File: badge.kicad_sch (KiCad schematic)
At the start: 26 parts, among them J1 SAO V.1.69bis master, SW1 power, SW2 SW_Push, SW3 update epaper, U1 Seeed XIAO ESP32-C3, U2 epaper2.13, U3 5V boost converter, U4 TXS0104EPWR

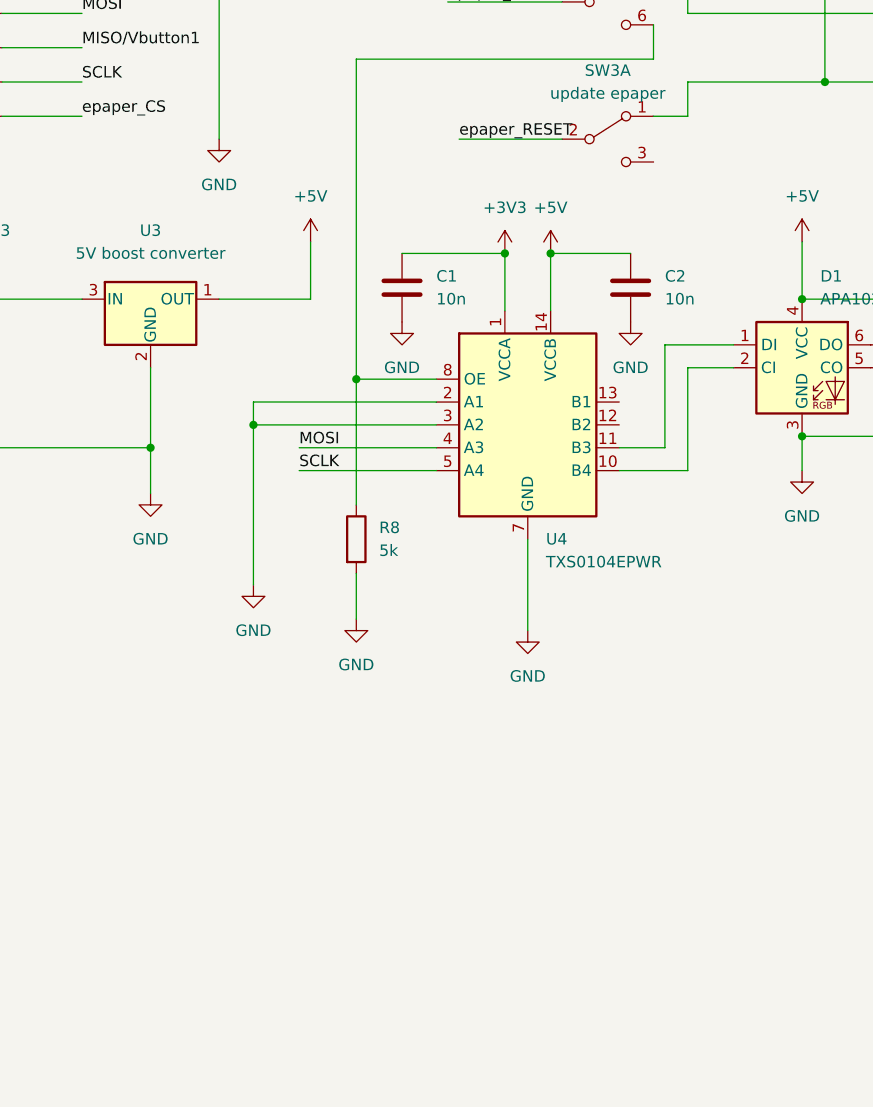
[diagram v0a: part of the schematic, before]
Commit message: added simple LED output
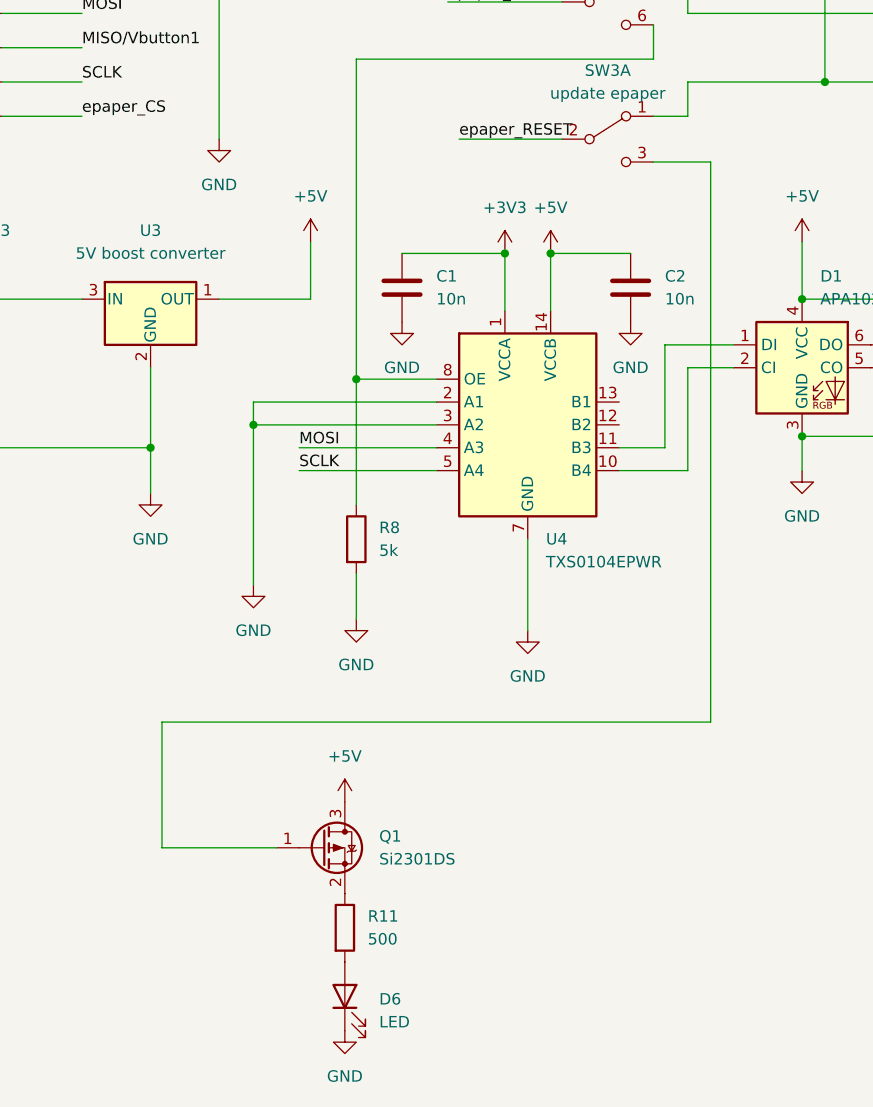
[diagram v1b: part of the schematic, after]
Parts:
- added D6: LED, LED_THT:LED_D5.0mm, symbol Device:LED
- added Q1: Si2301DS, Package_TO_SOT_SMD:SOT-23, symbol Device:Q_PMOS_GSD
- added R11: 500, Resistor_SMD:R_2010_5025Metric_Pad1.40x2.65mm_HandSolder, symbol Device:R
- D1, D2, D3, D4, D5: footprint LED_SMD:LED-APA102-2020 -> extra:LED-APA102-2020
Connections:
- net +5V: now also Q1.3 (D)
- net GND: now also D6.1 (K)
- net at SW3.3 (C): now also Q1.1 (G)
- new net: D6.2 (A), R11.2
- new net: Q1.2 (S), R11.1
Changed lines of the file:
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@@
+    (stroke (width 0) (type default) (color 0 0 0 0))
+  )
+  (wire (pts (xy 196.85 128.27) (xy 135.89 128.27))
     (stroke (width 0) (type default) (color 0 0 0 0))
   )
@@
     (stroke (width 0) (type default) (color 0 0 0 0))
   )
+  (wire (pts (xy 196.85 66.04) (xy 196.85 128.27))
+    (stroke (width 0) (type default) (color 0 0 0 0))
+  )
   (wire (pts (xy 207.01 74.93) (xy 207.01 81.28))
     (stroke (width 0) (type default) (color 0 0 0 0))
@@
     (stroke (width 0) (type default) (color 0 0 0 0))
   )
+  (wire (pts (xy 135.89 142.24) (xy 135.89 128.27))
+    (stroke (width 0) (type default) (color 0 0 0 0))
+  )
   (wire (pts (xy 194.31 88.9) (xy 199.39 88.9))
     (stroke (width 0) (type default) (color 0 0 0 0))
@@
     (stroke (width 0) (type default) (color 0 0 0 0))
   )
+  (wire (pts (xy 148.59 142.24) (xy 135.89 142.24))
+    (stroke (width 0) (type default) (color 0 0 0 0))
+  )
   (wire (pts (xy 146.05 92.71) (xy 146.05 95.25))
     (stroke (width 0) (type default) (color 0 0 0 0))
   )
   (wire (pts (xy 26.67 34.29) (xy 26.67 57.15))
+    (stroke (width 0) (type default) (color 0 0 0 0))
+  )
+  (wire (pts (xy 190.5 66.04) (xy 196.85 66.04))
     (stroke (width 0) (type default) (color 0 0 0 0))
   )
@@
     )
     (pin "1")
+  )
+  (symbol (lib_id "Device:LED") (at 156.21 158.75 90) (unit 1)
+    (in_bom yes) (on_board yes) (fields_autoplaced)
+    (property "Reference" "D6" (id 0) (at 160.02 159.0674 90)
+      (effects (font (size 1.27 1.27)) (justify right))
+    )
+    (property "Value" "LED" (id 1) (at 160.02 161.6074 90)
+      (effects (font (size 1.27 1.27)) (justify right))
+    )
+    (property "Footprint" "LED_THT:LED_D5.0mm" (id 2) (at 156.21 158.75 0)
+      (effects (font (size 1.27 1.27)) hide)
+    )
+    (property "Datasheet" "~" (id 3) (at 156.21 158.75 0)
+      (effects (font (size 1.27 1.27)) hide)
+    )
+    (pin "1")
+    (pin "2")
   )
   (symbol (lib_id "power:GND") (at 39.37 149.86 0) (unit 1)
@@
       (effects (font (size 1.27 1.27)) (justify left))
     )
-    (property "Footprint" "LED_SMD:LED-APA102-2020" (id 2) (at 238.76 96.52 0)
+    (property "Footprint" "extra:LED-APA102-2020" (id 2) (at 238.76 96.52 0)
       (effects (font (size 1.27 1.27)) (justify left top) hide)
     )
@@
     (pin "2")
   )
+  (symbol (lib_id "power:GND") (at 156.21 162.56 0) (unit 1)
+    (in_bom yes) (on_board yes) (fields_autoplaced)
+    (property "Reference" "#PWR022" (id 0) (at 156.21 168.91 0)
+      (effects (font (size 1.27 1.27)) hide)
+    )
+    (property "Value" "GND" (id 1) (at 156.21 167.64 0))
+    (property "Footprint" "" (id 2) (at 156.21 162.56 0)
+      (effects (font (size 1.27 1.27)) hide)
+    )
+    (property "Datasheet" "" (id 3) (at 156.21 162.56 0)
+      (effects (font (size 1.27 1.27)) hide)
+    )
+    (pin "1")
+  )
   (symbol (lib_id "power:+5V") (at 179.07 76.2 0) (unit 1)
     (in_bom yes) (on_board yes) (fields_autoplaced)
@@
     )
     (pin "1")
+  )
+  (symbol (lib_id "Device:R") (at 156.21 151.13 0) (unit 1)
+    (in_bom yes) (on_board yes) (fields_autoplaced)
+    (property "Reference" "R11" (id 0) (at 158.75 149.8599 0)
+      (effects (font (size 1.27 1.27)) (justify left))
+    )
+    (property "Value" "500" (id 1) (at 158.75 152.3999 0)
+      (effects (font (size 1.27 1.27)) (justify left))
+    )
+    (property "Footprint" "Resistor_SMD:R_2010_5025Metric_Pad1.40x2.65mm_HandSolder" (id 2) (at 154.432 151.13 90)
+      (effects (font (size 1.27 1.27)) hide)
+    )
+    (property "Datasheet" "~" (id 3) (at 156.21 151.13 0)
+      (effects (font (size 1.27 1.27)) hide)
+    )
+    (pin "1")
+    (pin "2")
   )
   (symbol (lib_id "power:GND") (at 207.01 100.33 0) (unit 1)
@@
     (pin "8")
   )
+  (symbol (lib_id "power:+5V") (at 156.21 137.16 0) (unit 1)
+    (in_bom yes) (on_board yes) (fields_autoplaced)
+    (property "Reference" "#PWR012" (id 0) (at 156.21 140.97 0)
+      (effects (font (size 1.27 1.27)) hide)
+    )
+    (property "Value" "+5V" (id 1) (at 156.21 132.08 0))
+    (property "Footprint" "" (id 2) (at 156.21 137.16 0)
+      (effects (font (size 1.27 1.27)) hide)
+    )
+    (property "Datasheet" "" (id 3) (at 156.21 137.16 0)
+      (effects (font (size 1.27 1.27)) hide)
+    )
+    (pin "1")
+  )
   (symbol (lib_id "power:GND") (at 146.05 113.03 0) (unit 1)
     (in_bom yes) (on_board yes)
@@
       (effects (font (size 1.27 1.27)) (justify left))
     )
-    (property "Footprint" "LED_SMD:LED-APA102-2020" (id 2) (at 208.28 96.52 0)
+    (property "Footprint" "extra:LED-APA102-2020" (id 2) (at 208.28 96.52 0)
       (effects (font (size 1.27 1.27)) (justify left top) hide)
     )
@@
       (effects (font (size 1.27 1.27)) (justify left))
     )
-    (property "Footprint" "LED_SMD:LED-APA102-2020" (id 2) (at 254 96.52 0)
+    (property "Footprint" "extra:LED-APA102-2020" (id 2) (at 254 96.52 0)
       (effects (font (size 1.27 1.27)) (justify left top) hide)
     )
@@
       (effects (font (size 1.27 1.27)) (justify left))
     )
-    (property "Footprint" "LED_SMD:LED-APA102-2020" (id 2) (at 269.24 96.52 0)
+    (property "Footprint" "extra:LED-APA102-2020" (id 2) (at 269.24 96.52 0)
       (effects (font (size 1.27 1.27)) (justify left top) hide)
     )
@@
       (effects (font (size 1.27 1.27)) (justify left))
     )
-    (property "Footprint" "LED_SMD:LED-APA102-2020" (id 2) (at 223.52 96.52 0)
+    (property "Footprint" "extra:LED-APA102-2020" (id 2) (at 223.52 96.52 0)
       (effects (font (size 1.27 1.27)) (justify left top) hide)
     )
@@
     )
     (pin "1")
+  )
+  (symbol (lib_id "Device:Q_PMOS_GSD") (at 153.67 142.24 0) (unit 1)
+    (in_bom yes) (on_board yes) (fields_autoplaced)
+    (property "Reference" "Q1" (id 0) (at 160.02 140.9699 0)
+      (effects (font (size 1.27 1.27)) (justify left))
+    )
+    (property "Value" "Si2301DS" (id 1) (at 160.02 143.5099 0)
+      (effects (font (size 1.27 1.27)) (justify left))
+    )
+    (property "Footprint" "Package_TO_SOT_SMD:SOT-23" (id 2) (at 158.75 139.7 0)
+      (effects (font (size 1.27 1.27)) hide)
+    )
+    (property "Datasheet" "~" (id 3) (at 153.67 142.24 0)
+      (effects (font (size 1.27 1.27)) hide)
+    )
+    (pin "1")
+    (pin "2")
+    (pin "3")
   )
   (symbol (lib_id "Switch:SW_DPDT_x2") (at 38.1 100.33 0) (unit 2)
@@
       (reference "#PWR011") (unit 1) (value "+3V3") (footprint "")
     )
+    (path "/8f2e9747-4605-475d-a813-8fb15e74adb0"
+      (reference "#PWR012") (unit 1) (value "+5V") (footprint "")
+    )
     (path "/278915d1-0ba2-460e-9183-c0619581d023"
       (reference "#PWR013") (unit 1) (value "+5V") (footprint "")
@@
       (reference "#PWR021") (unit 1) (value "+5V") (footprint "")
     )
+    (path "/4a66934a-f0bf-4f03-a56c-02301dcabcbe"
+      (reference "#PWR022") (unit 1) (value "GND") (footprint "")
+    )
     (path "/1259210b-f4fa-41bd-a422-f3e7b70ae6a3"
       (reference "#PWR023") (unit 1) (value "+5V") (footprint "")
@@
     )
     (path "/965b81fc-cc69-41b0-8930-90de11ba59ea"
-      (reference "D1") (unit 1) (value "APA102") (footprint "LED_SMD:LED-APA102-2020")
+      (reference "D1") (unit 1) (value "APA102") (footprint "extra:LED-APA102-2020")
     )
     (path "/d3f450b1-e2bd-4d35-a3d2-5e68df095604"
-      (reference "D2") (unit 1) (value "APA102") (footprint "LED_SMD:LED-APA102-2020")
+      (reference "D2") (unit 1) (value "APA102") (footprint "extra:LED-APA102-2020")
     )
     (path "/27341a41-1293-4206-a44e-4918c0b1f1f0"
-      (reference "D3") (unit 1) (value "APA102") (footprint "LED_SMD:LED-APA102-2020")
+      (reference "D3") (unit 1) (value "APA102") (footprint "extra:LED-APA102-2020")
     )
     (path "/9d74b5b2-0db6-4256-8077-177e9e321141"
-      (reference "D4") (unit 1) (value "APA102") (footprint "LED_SMD:LED-APA102-2020")
+      (reference "D4") (unit 1) (value "APA102") (footprint "extra:LED-APA102-2020")
     )
     (path "/bd236e9e-87b9-44a0-8fc0-ca84e57e89b4"
-      (reference "D5") (unit 1) (value "APA102") (footprint "LED_SMD:LED-APA102-2020")
+      (reference "D5") (unit 1) (value "APA102") (footprint "extra:LED-APA102-2020")
+    )
+    (path "/128cfbd9-ecc7-4a80-944b-096a6c28c868"
+      (reference "D6") (unit 1) (value "LED") (footprint "LED_THT:LED_D5.0mm")
     )
     (path "/82a433df-4332-496a-b45e-90f02e019617"
       (reference "J1") (unit 1) (value "SAO V.1.69bis master") (footprint "Connector_IDC:IDC-Header_2x03_P2.54mm_Vertical")
     )
+    (path "/db794ee2-aa5a-47d1-a914-b3ebb8b825c6"
+      (reference "Q1") (unit 1) (value "Si2301DS") (footprint "Package_TO_SOT_SMD:SOT-23")
+    )
     (path "/51f7f983-853a-452a-8ab7-c02921f8eb56"
       (reference "R1") (unit 1) (value "50k") (footprint "Resistor_SMD:R_2010_5025Metric_Pad1.40x2.65mm_HandSolder")
@@
       (reference "R10") (unit 1) (value "50k") (footprint "Resistor_SMD:R_2010_5025Metric_Pad1.40x2.65mm_HandSolder")
     )
+    (path "/71e822d1-6290-4d27-b0af-d53ba7897ba1"
+      (reference "R11") (unit 1) (value "500") (footprint "Resistor_SMD:R_2010_5025Metric_Pad1.40x2.65mm_HandSolder")
+    )
     (path "/1ad19a07-7043-4709-a6b6-93f957e89d4c"

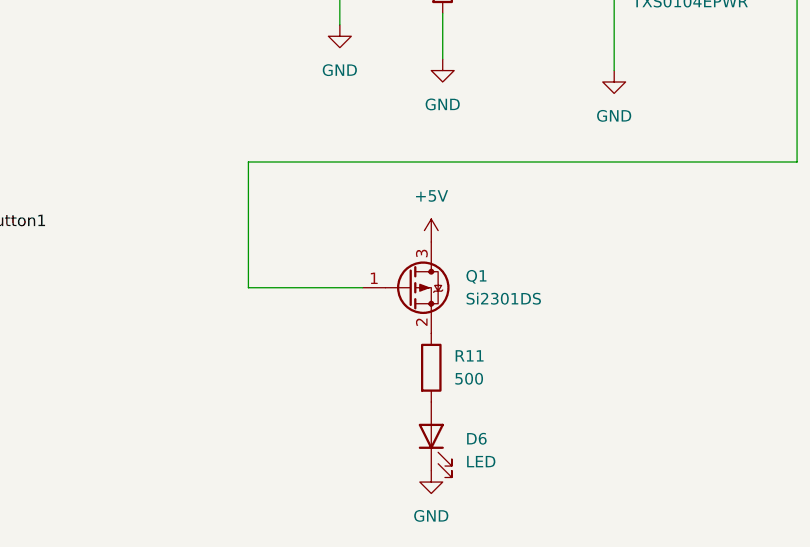
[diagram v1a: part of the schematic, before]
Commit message: drive LED with N-MOSFET
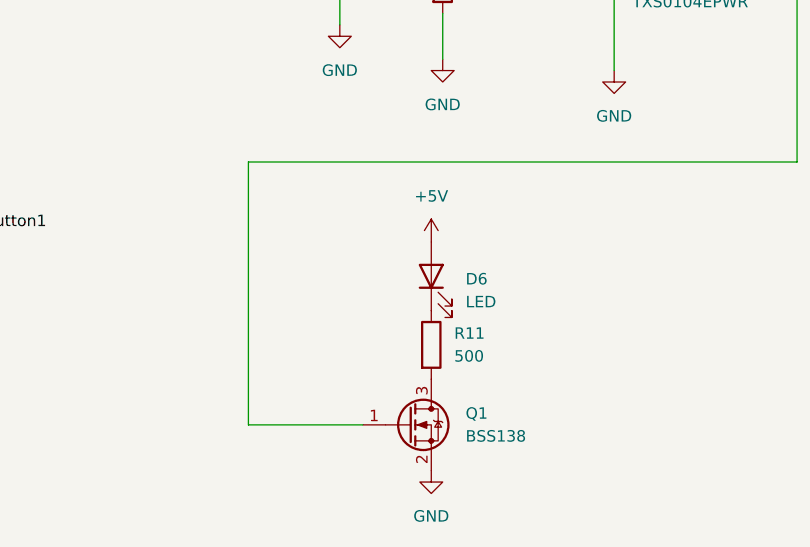
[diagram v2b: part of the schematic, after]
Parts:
- removed Q1: Si2301DS, Package_TO_SOT_SMD:SOT-23, symbol Device:Q_PMOS_GSD
- added Q1: BSS138, Package_TO_SOT_SMD:SOT-23, symbol Device:Q_NMOS_GSD
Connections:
- net +5V: now also D6.2 (A)
- net GND: now also Q1.2 (S); no longer D6.1 (K)
- net at R11.2: now also Q1.3 (D); no longer D6.2 (A)
- net at R11.1: now also D6.1 (K)
- net at SW3.3 (C): now also Q1.1 (G)
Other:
- moved on the sheet: D6, R11
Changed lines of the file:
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@@
     (stroke (width 0) (type default) (color 0 0 0 0))
   )
-  (wire (pts (xy 135.89 142.24) (xy 135.89 128.27))
+  (wire (pts (xy 135.89 157.48) (xy 135.89 128.27))
     (stroke (width 0) (type default) (color 0 0 0 0))
   )
@@
     (stroke (width 0) (type default) (color 0 0 0 0))
   )
-  (wire (pts (xy 148.59 142.24) (xy 135.89 142.24))
+  (wire (pts (xy 148.59 157.48) (xy 135.89 157.48))
     (stroke (width 0) (type default) (color 0 0 0 0))
   )
@@
     (pin "1")
   )
-  (symbol (lib_id "Device:LED") (at 156.21 158.75 90) (unit 1)
-    (in_bom yes) (on_board yes) (fields_autoplaced)
-    (property "Reference" "D6" (id 0) (at 160.02 159.0674 90)
+  (symbol (lib_id "Device:LED") (at 156.21 140.97 90) (unit 1)
+    (in_bom yes) (on_board yes) (fields_autoplaced)
+    (property "Reference" "D6" (id 0) (at 160.02 141.2874 90)
       (effects (font (size 1.27 1.27)) (justify right))
     )
-    (property "Value" "LED" (id 1) (at 160.02 161.6074 90)
+    (property "Value" "LED" (id 1) (at 160.02 143.8274 90)
       (effects (font (size 1.27 1.27)) (justify right))
     )
-    (property "Footprint" "LED_THT:LED_D5.0mm" (id 2) (at 156.21 158.75 0)
-      (effects (font (size 1.27 1.27)) hide)
-    )
-    (property "Datasheet" "~" (id 3) (at 156.21 158.75 0)
+    (property "Footprint" "LED_THT:LED_D5.0mm" (id 2) (at 156.21 140.97 0)
+      (effects (font (size 1.27 1.27)) hide)
+    )
+    (property "Datasheet" "~" (id 3) (at 156.21 140.97 0)
       (effects (font (size 1.27 1.27)) hide)
     )
@@
     (pin "1")
   )
-  (symbol (lib_id "Device:R") (at 156.21 151.13 0) (unit 1)
-    (in_bom yes) (on_board yes) (fields_autoplaced)
-    (property "Reference" "R11" (id 0) (at 158.75 149.8599 0)
-      (effects (font (size 1.27 1.27)) (justify left))
-    )
-    (property "Value" "500" (id 1) (at 158.75 152.3999 0)
-      (effects (font (size 1.27 1.27)) (justify left))
-    )
-    (property "Footprint" "Resistor_SMD:R_2010_5025Metric_Pad1.40x2.65mm_HandSolder" (id 2) (at 154.432 151.13 90)
-      (effects (font (size 1.27 1.27)) hide)
-    )
-    (property "Datasheet" "~" (id 3) (at 156.21 151.13 0)
+  (symbol (lib_id "Device:R") (at 156.21 148.59 0) (unit 1)
+    (in_bom yes) (on_board yes) (fields_autoplaced)
+    (property "Reference" "R11" (id 0) (at 158.75 147.3199 0)
+      (effects (font (size 1.27 1.27)) (justify left))
+    )
+    (property "Value" "500" (id 1) (at 158.75 149.8599 0)
+      (effects (font (size 1.27 1.27)) (justify left))
+    )
+    (property "Footprint" "Resistor_SMD:R_2010_5025Metric_Pad1.40x2.65mm_HandSolder" (id 2) (at 154.432 148.59 90)
+      (effects (font (size 1.27 1.27)) hide)
+    )
+    (property "Datasheet" "~" (id 3) (at 156.21 148.59 0)
       (effects (font (size 1.27 1.27)) hide)
     )
@@
     (pin "1")
   )
+  (symbol (lib_id "Device:Q_NMOS_GSD") (at 153.67 157.48 0) (unit 1)
+    (in_bom yes) (on_board yes) (fields_autoplaced)
+    (property "Reference" "Q1" (id 0) (at 160.02 156.2099 0)
+      (effects (font (size 1.27 1.27)) (justify left))
+    )
+    (property "Value" "BSS138" (id 1) (at 160.02 158.7499 0)
+      (effects (font (size 1.27 1.27)) (justify left))
+    )
+    (property "Footprint" "Package_TO_SOT_SMD:SOT-23" (id 2) (at 158.75 154.94 0)
+      (effects (font (size 1.27 1.27)) hide)
+    )
+    (property "Datasheet" "~" (id 3) (at 153.67 157.48 0)
+      (effects (font (size 1.27 1.27)) hide)
+    )
+    (pin "1")
+    (pin "2")
+    (pin "3")
+  )
   (symbol (lib_id "LED:APA102") (at 267.97 88.9 0) (unit 1)
     (in_bom yes) (on_board yes) (fields_autoplaced)
@@
     )
     (pin "1")
-  )
-  (symbol (lib_id "Device:Q_PMOS_GSD") (at 153.67 142.24 0) (unit 1)
-    (in_bom yes) (on_board yes) (fields_autoplaced)
-    (property "Reference" "Q1" (id 0) (at 160.02 140.9699 0)
-      (effects (font (size 1.27 1.27)) (justify left))
-    )
-    (property "Value" "Si2301DS" (id 1) (at 160.02 143.5099 0)
-      (effects (font (size 1.27 1.27)) (justify left))
-    )
-    (property "Footprint" "Package_TO_SOT_SMD:SOT-23" (id 2) (at 158.75 139.7 0)
-      (effects (font (size 1.27 1.27)) hide)
-    )
-    (property "Datasheet" "~" (id 3) (at 153.67 142.24 0)
-      (effects (font (size 1.27 1.27)) hide)
-    )
-    (pin "1")
-    (pin "2")
-    (pin "3")
   )
   (symbol (lib_id "Switch:SW_DPDT_x2") (at 38.1 100.33 0) (unit 2)
@@
       (reference "J1") (unit 1) (value "SAO V.1.69bis master") (footprint "Connector_IDC:IDC-Header_2x03_P2.54mm_Vertical")
     )
-    (path "/db794ee2-aa5a-47d1-a914-b3ebb8b825c6"
-      (reference "Q1") (unit 1) (value "Si2301DS") (footprint "Package_TO_SOT_SMD:SOT-23")
+    (path "/b727620f-4ada-4b98-9c2f-d493d3e466ca"
+      (reference "Q1") (unit 1) (value "BSS138") (footprint "Package_TO_SOT_SMD:SOT-23")
     )
     (path "/51f7f983-853a-452a-8ab7-c02921f8eb56"
